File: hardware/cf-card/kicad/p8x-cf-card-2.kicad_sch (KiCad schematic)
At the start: 2 parts, among them U10 74HCT245, U11 74HCT10

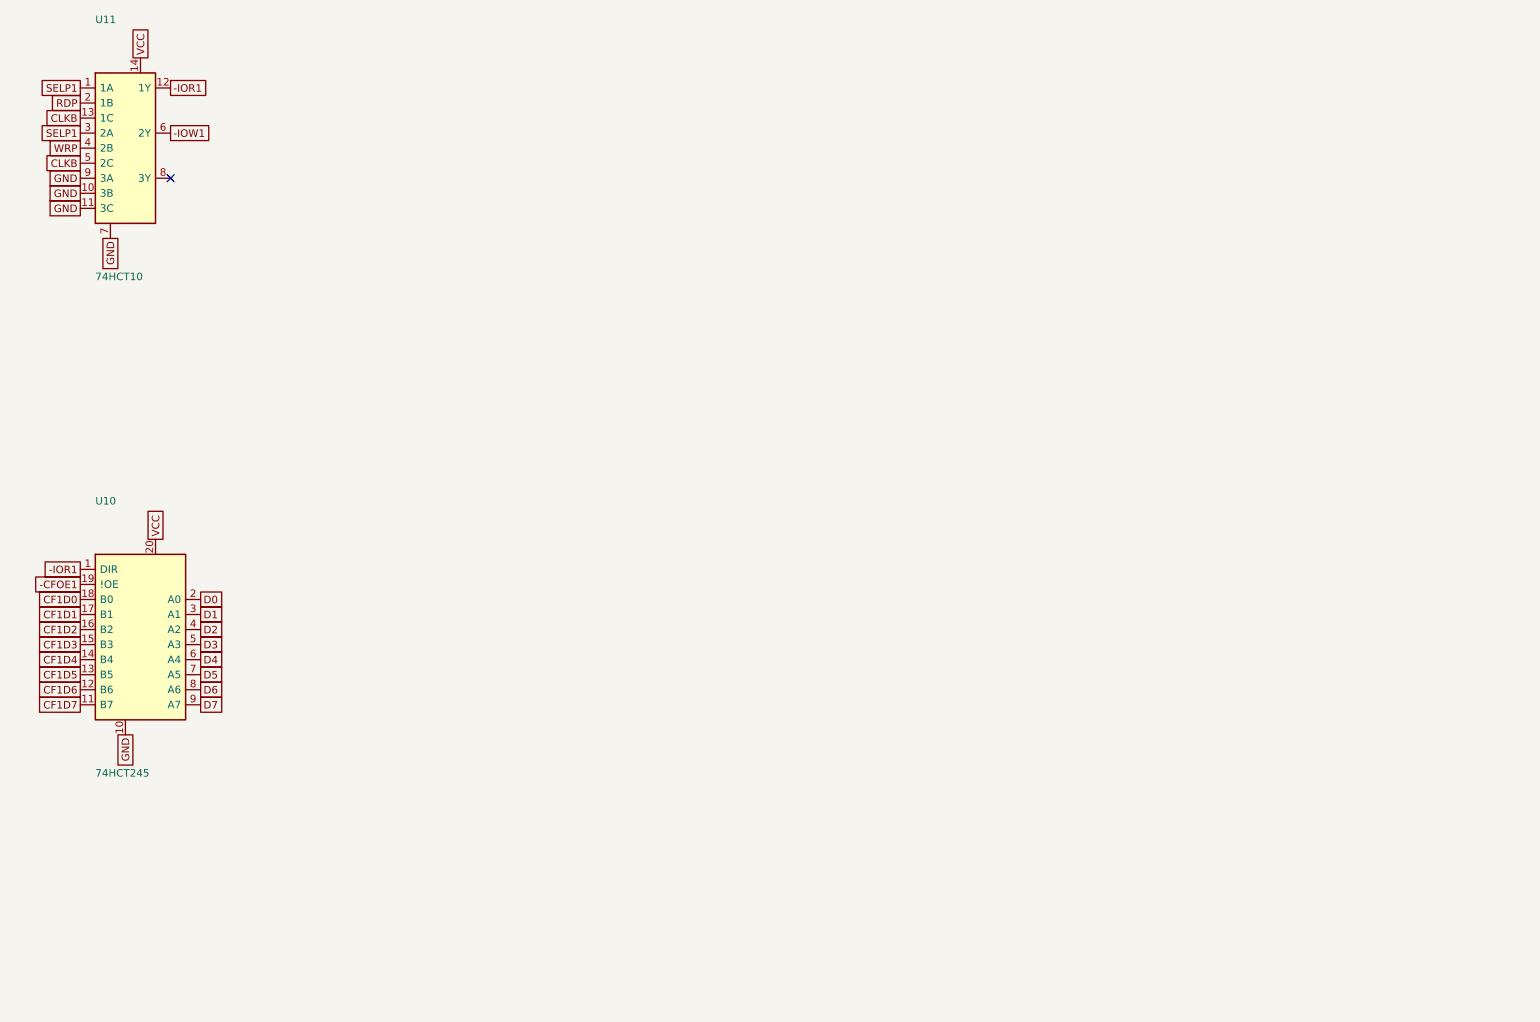
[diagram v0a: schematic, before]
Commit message: feat(sch): draw every P8X card schematic by function
Extend the functional-sheet grouping from the io-card to the control,
regbank, alu, memory, cf, ps2 and bustest cards. functional_sheets now
attaches unnamed glue gates, LEDs, resistors and connectors to the block
they share the most local nets with, so each block lists only its main
parts. A net with two or more pins on a sheet is now wired there even if
it continues elsewhere (its global name label rides on the wire), and
every wire is oriented by drawing side. The regbank gets one pointer per
sheet; the ps2 latches share a sheet with the AVR so the mailbox bus is
drawn. The bustest probe resistors use a straight-order RNISO8DSTR
drawing (the reversed B side forced every wire to cross and the sheet
fell back to labels). build_sch.sh now shows ELK fallbacks and clears old
numbered sheets before a build. All eight netlists match the boards,
ERC 0 errors; the boards change only in footprint link paths.

Co-Authored-By: Claude Opus 5.5 <noreply@anthropic.com>
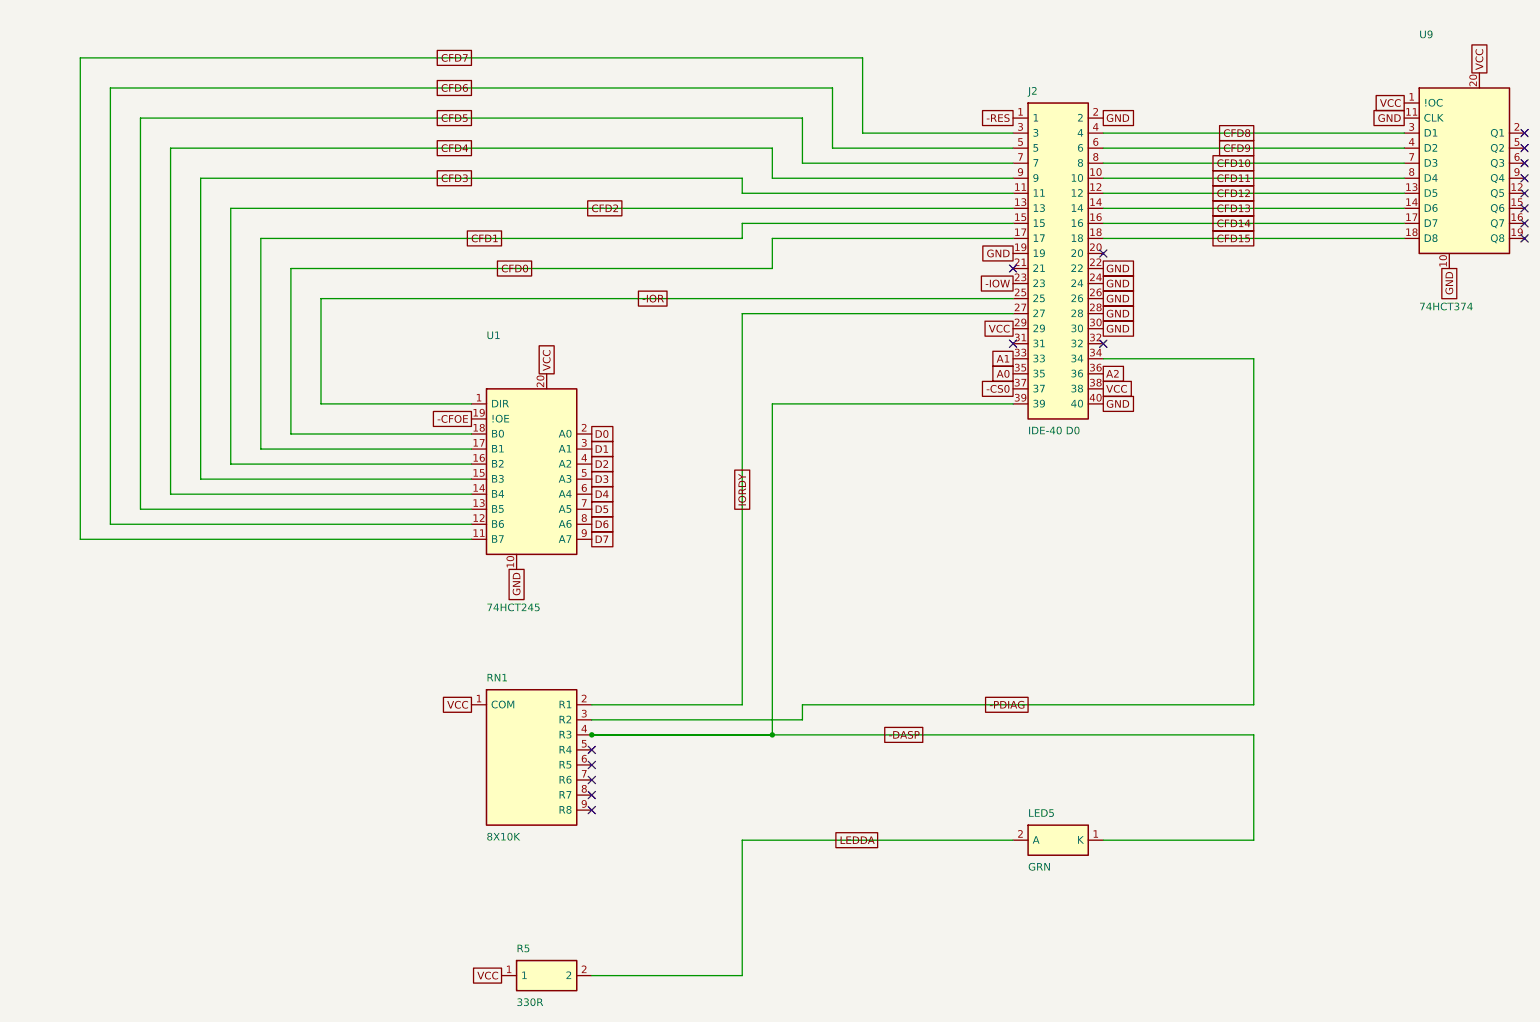
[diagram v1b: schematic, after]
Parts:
- removed U10: 74HCT245, Package_DIP:DIP-20_W7.62mm, symbol p8x:74245
- removed U11: 74HCT10, Package_DIP:DIP-14_W7.62mm, symbol p8x:7410
- added J2: IDE-40 D0, Connector_IDC:IDC-Header_2x20_P2.54mm_Vertical, symbol p8x:IDE40
- added LED5: GRN, LED_THT:LED_D5.0mm, symbol p8x:LED
- added R5: 330R, Resistor_THT:R_Axial_DIN0207_L6.3mm_D2.5mm_P10.16mm_Horizontal, symbol p8x:RES
- added RN1: 8X10K, Resistor_THT:R_Array_SIP9, symbol p8x:SIP9
- added U1: 74HCT245, Package_DIP:DIP-20_W7.62mm, symbol p8x:74245
- added U9: 74HCT374, Package_DIP:DIP-20_W7.62mm, symbol p8x:74374
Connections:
- net D0: now also U1.2 (A0)
- net D1: now also U1.3 (A1)
- net D2: now also U1.4 (A2)
- net D3: now also U1.5 (A3)
- net D4: now also U1.6 (A4)
- net D5: now also U1.7 (A5)
- net D6: now also U1.8 (A6)
- net D7: now also U1.9 (A7)
- net GND: now also J2.19, J2.2, J2.22, J2.24, J2.26, J2.28, J2.30, J2.40, U1.10, U9.10, U9.11 (CLK)
- net VCC: now also J2.29, J2.38, R5.1, RN1.1 (COM), U1.20, U9.1 (!OC), U9.20
- new net -CFOE: U1.19 (!OE)
- new net -CS0: J2.37
- new net -DASP: J2.39, LED5.1 (K), RN1.4 (R3)
- new net -IOR: J2.25, U1.1 (DIR)
- new net -IOW: J2.23
- new net -PDIAG: J2.34, RN1.3 (R2)
- new net -RES: J2.1
- new net A0: J2.35
- new net A1: J2.33
- new net A2: J2.36
- new net CFD0: J2.17, U1.18 (B0)
- new net CFD1: J2.15, U1.17 (B1)
- new net CFD10: J2.8, U9.7 (D3)
- new net CFD11: J2.10, U9.8 (D4)
- new net CFD12: J2.12, U9.13 (D5)
- new net CFD13: J2.14, U9.14 (D6)
- new net CFD14: J2.16, U9.17 (D7)
- new net CFD15: J2.18, U9.18 (D8)
- new net CFD2: J2.13, U1.16 (B2)
- new net CFD3: J2.11, U1.15 (B3)
- new net CFD4: J2.9, U1.14 (B4)
- new net CFD5: J2.7, U1.13 (B5)
- new net CFD6: J2.5, U1.12 (B6)
- new net CFD7: J2.3, U1.11 (B7)
- new net CFD8: J2.4, U9.3 (D1)
- new net CFD9: J2.6, U9.4 (D2)
- new net IORDY: J2.27, RN1.2 (R1)
- new net LEDDA: LED5.2 (A), R5.2
- no-connect marks 1 -> 17
